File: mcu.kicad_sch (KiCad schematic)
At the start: 1 part, among them IC1 ATSAMD21G18A-AFT

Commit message: Add MCU stuff, cortex debug connector and docs
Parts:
- added C10, C12, C13: 0.1u, symbol Device:C
- added C11, C15: 10u, symbol Device:C
- added C14: 1u, symbol Device:C
- added FB1: FerriteBead, symbol Device:FerriteBead
- added J1: FTSH-105-XX-X-DV, bldc-driver-pcb:SAMTEC_FTSH-105-XX-X-DV, symbol bldc-driver-pcb:FTSH-105-XX-X-DV
- added R28: 1k, symbol Device:R_Small_US
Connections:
- net VDDIN is gone; now on net +3V3: IC1.44 (VDDIN)
- net VDDIO is gone; now on net +3V3: IC1.17 (VDDIO_1), IC1.36 (VDDIO_2)
- net GND: now also C10.2, C11.2, C12.2, C13.2, C14.2, C15.2, J1.03, J1.05
- net RESET: now also J1.10
- net SWCLK: now also J1.04, R28.2
- net SWDIO: now also J1.02
- net VDDANA: now also C10.1, C11.1, FB1.2
- net XIN32: now reaches IC1.1 (PA00)
- net XOUT32: now reaches IC1.2 (PA01)
- net XIN: now reaches IC1.23 (PA14)
- net XOUT: now reaches IC1.24 (PA15)
- net SERCOM1_PAD0: now reaches IC1.25 (PA16)
- net SERCOM1_PAD1: now reaches IC1.26 (PA17)
- net SERCOM1_PAD2: now reaches IC1.27 (PA18)
- net SERCOM1_PAD3: now reaches IC1.28 (PA19)
- net SERCOM3_PAD0: now reaches IC1.31 (PA22)
- net SERCOM3_PAD1: now reaches IC1.32 (PA23)
- net USB_D-: now reaches IC1.33 (PA24)
- net USB_D+: now reaches IC1.34 (PA25)
- net ENCODER_CSn: now reaches IC1.37 (PB22)
- net DRV8316_CSn: now reaches IC1.38 (PB23)
- net DBG_LED_GREEN: now reaches IC1.39 (PA27)
- net ADC_VREFA: now reaches IC1.4 (PA03)
- net DBG_LED_RED: now reaches IC1.41 (PA28)
- net VDDCORE renamed +3V3
- net +3V3: now also C12.1, C13.1, C14.1, C15.1, FB1.1, J1.01, R28.1
- no-connect marks 2 -> 10
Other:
- note added: "Can also be SERCOM5_PAD3 and PAD2"
- note added: "Close to device pins"
- note added: "Cortex Debug Connector"
- note added: "MOSI on PAD0 SCK on PAD1 MISO on PAD3"
- note added: "Power Supply Connections"
- note added: "Programming/Debugging"
- moved on the sheet: IC1

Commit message: Add gitignore
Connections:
- net +3V3: no longer C12.1, C13.1, C14.1, C15.1, FB1.1, IC1.17 (VDDIO_1), IC1.36 (VDDIO_2), IC1.43 (VDDCORE), IC1.44 (VDDIN)
- net SERCOM5_PAD2: now reaches IC1.29 (PA20)
- net SERCOM5_PAD3: now reaches IC1.30 (PA21)
- new net 3V3_MCU: C12.1, C13.1, C14.1, C15.1, FB1.1, IC1.17 (VDDIO_1), IC1.36 (VDDIO_2), IC1.43 (VDDCORE), IC1.44 (VDDIN)
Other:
- note removed: "Can also be SERCOM5_PAD3 and PAD2"
- note removed: "MOSI on PAD0 SCK on PAD1 MISO on PAD3"

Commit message: Initial routing
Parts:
- added J3: G125-MH11205L1P, Sandbox:G125-MH11205L1P, symbol Sandbox:G125-MH11205L1P
- added J4: USB3135-XX-X_REVB, bldc-driver-pcb:GCT_USB3135-XX-X_REVB, symbol bldc-driver-pcb:USB3135-XX-X_REVB
- C10, C11, C12, C13, C14, C15: footprint (none) -> Capacitor_SMD:C_0603_1608Metric
- FB1: footprint (none) -> Inductor_SMD:L_0603_1608Metric
- R28: footprint (none) -> Resistor_SMD:R_0603_1608Metric
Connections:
- net +3V3: now also J3.11, J3.12
- net 3V3_MCU: no longer C14.1, IC1.43 (VDDCORE)
- net DRV8316_CSn: now also J3.7
- net GND: now also J3.10, J3.2, J3.4, J3.8, J3.9, J4.4 (ID), J4.5 (GND)
- net SERCOM3_PAD0: now also J3.3
- net SERCOM3_PAD1: now also J3.1
- net SERCOM5_PAD2: now also J3.6
- net SERCOM5_PAD3: now also J3.5
- net USB_D+: now also J4.3 (D+)
- net USB_D-: now also J4.2 (D-)
- new net: J4.6 (SHIELD), J4.7 (SHIELD), J4.8 (SHIELD), J4.9 (SHIELD)
- new net +5V: J4.1 (VBUS)
- new net VDDCORE: C14.1, IC1.43 (VDDCORE)
- no-connect marks 10 -> 12

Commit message: More routing
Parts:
- added C16: 0.1u, Capacitor_SMD:C_0402_1005Metric, symbol Device:C
- C10, C11, C12, C13, C14: footprint Capacitor_SMD:C_0603_1608Metric -> Capacitor_SMD:C_0402_1005Metric
- FB1: footprint Inductor_SMD:L_0603_1608Metric -> Inductor_SMD:L_0402_1005Metric
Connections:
- net 3V3_MCU: now also C16.1
- net GND: now also C16.2
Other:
- moved on the sheet: C12, C13, C15

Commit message: Finalize layout -- VREF pending
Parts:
- removed J3: G125-MH11205L1P, Sandbox:G125-MH11205L1P, symbol Sandbox:G125-MH11205L1P
- removed J4: USB3135-XX-X_REVB, bldc-driver-pcb:GCT_USB3135-XX-X_REVB, symbol bldc-driver-pcb:USB3135-XX-X_REVB
- added J7: USB3140-30-0170-1-C, bldc-driver-pcb:USB31403001700C, symbol bldc-driver-pcb:USB3140-30-0170-1-C
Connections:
- net XOUT is gone; now on net ENCODER_CSn: IC1.24 (PA15)
- net +5V: now also J7.1 (VBUS)
- net ENCODER_CSn: no longer IC1.37 (PB22)
- net GND: now also J7.4 (ID), J7.5 (GND), J7.MH2
- net USB_D+: now also J7.3 (D+)
- net USB_D-: now also J7.2 (D-)
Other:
- note added: "Low-Impedance path to GND Investigate 0.1uF//1MΩ"
- note added: "Tie ID pin to GND"

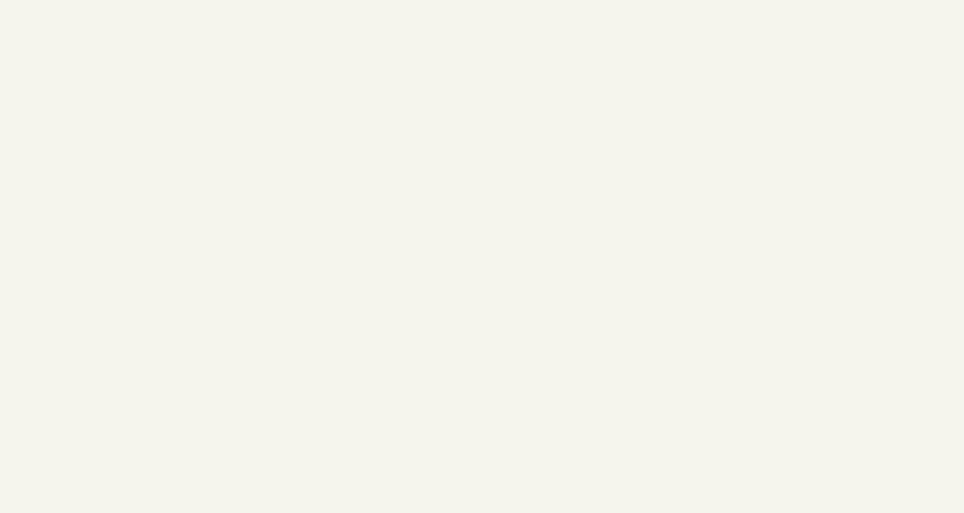
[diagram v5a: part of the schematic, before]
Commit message: Add 32.768kHz external clock & specify ferrite bead part number
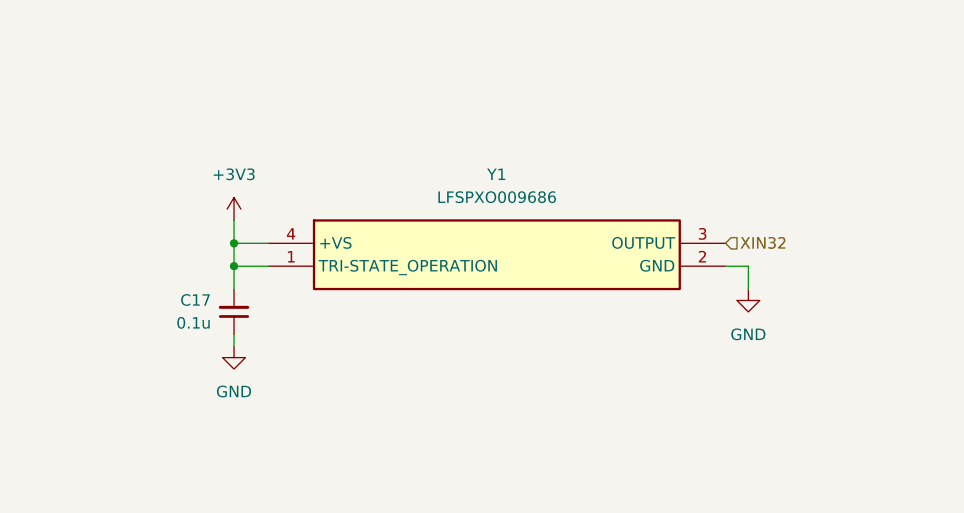
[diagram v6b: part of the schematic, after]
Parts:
- added C17: 0.1u, Capacitor_SMD:C_0603_1608Metric, symbol Device:C_Small
- added Y1: LFSPXO009686, bldc-driver-pcb:LFSPXO009686, symbol bldc-driver-pcb:LFSPXO009686
- FB1: footprint Inductor_SMD:L_0402_1005Metric -> bldc-driver-pcb:BLM18SP221SN1B; Manufacturer_Part_Number (none) -> BLM18SP221SN1B
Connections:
- net +3V3: now also C17.2, Y1.1 (TRI-STATE_OPERATION), Y1.4 (+VS)
- net GND: now also C17.1, Y1.2 (GND)
- net XIN32: now also Y1.3 (OUTPUT)
